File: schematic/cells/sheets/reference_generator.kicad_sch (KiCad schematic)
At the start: 10 parts, among them U1001 REF5050AIDR, U1004 OPA4197IPWR, U1007 OPA4197IPWR, U1010 OPA4197IPWR

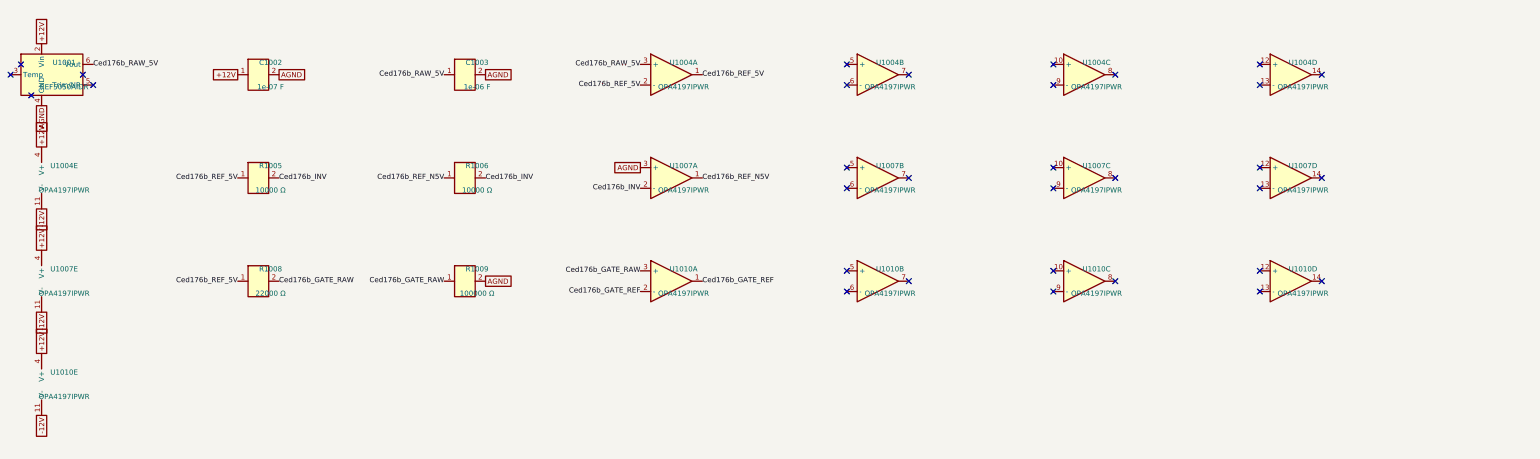
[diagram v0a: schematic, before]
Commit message: Close master schematic integration gates
Audit locked panel coverage, netlist parity, sensitive islands and all active units; terminate spare cells, refresh evidence, and record rail budget overshoot and draft exports.
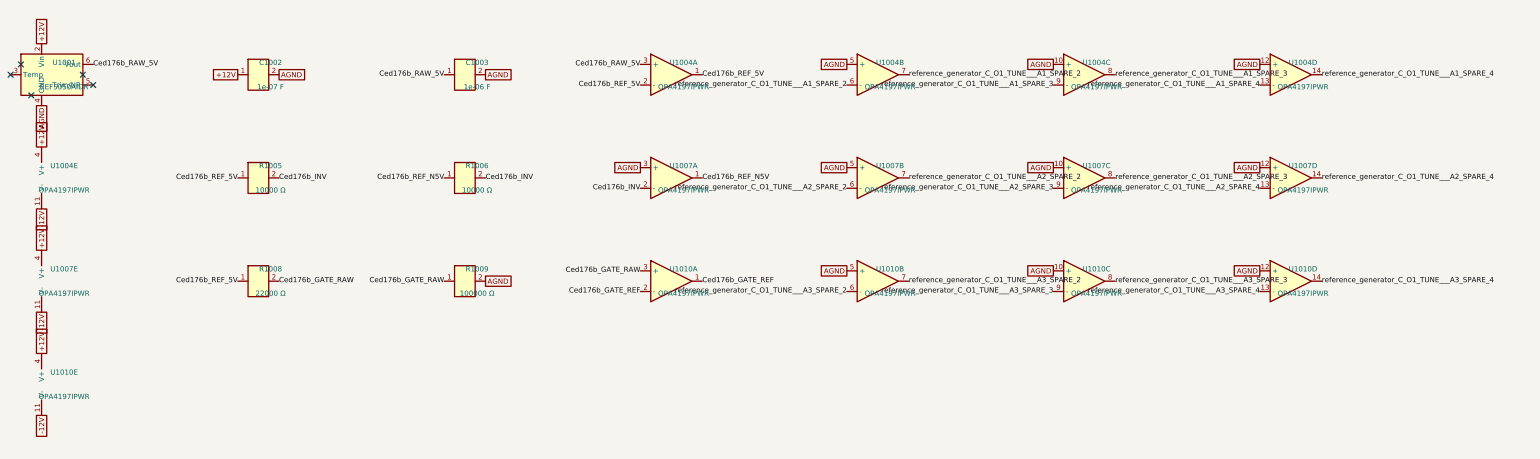
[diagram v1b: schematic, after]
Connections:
- net AGND: now also U1004.10 (+), U1004.12 (+), U1004.5 (+), U1007.10 (+), U1007.12 (+), U1007.5 (+), U1010.10 (+), U1010.12 (+), U1010.5 (+)
- net reference_generator_C_O1_TUNE___A1_SPARE_4: now reaches U1004.13 (-)
- net reference_generator_C_O1_TUNE___A1_SPARE_4: now also U1004.14
- net reference_generator_C_O1_TUNE___A2_SPARE_3: now reaches U1007.8
- net reference_generator_C_O1_TUNE___A2_SPARE_3: now also U1007.9 (-)
- net reference_generator_C_O1_TUNE___A3_SPARE_3: now reaches U1010.8
- net reference_generator_C_O1_TUNE___A3_SPARE_3: now also U1010.9 (-)
- net reference_generator_C_O1_TUNE___A2_SPARE_2: now reaches U1007.6 (-)
- net reference_generator_C_O1_TUNE___A2_SPARE_2: now also U1007.7
- net reference_generator_C_O1_TUNE___A1_SPARE_2: now reaches U1004.6 (-)
- net reference_generator_C_O1_TUNE___A1_SPARE_2: now also U1004.7
- net reference_generator_C_O1_TUNE___A1_SPARE_3: now reaches U1004.8
- net reference_generator_C_O1_TUNE___A1_SPARE_3: now also U1004.9 (-)
- net reference_generator_C_O1_TUNE___A3_SPARE_2: now reaches U1010.6 (-)
- net reference_generator_C_O1_TUNE___A3_SPARE_2: now also U1010.7
- net reference_generator_C_O1_TUNE___A2_SPARE_4: now reaches U1007.13 (-)
- net reference_generator_C_O1_TUNE___A2_SPARE_4: now also U1007.14
- net reference_generator_C_O1_TUNE___A3_SPARE_4: now reaches U1010.13 (-)
- net reference_generator_C_O1_TUNE___A3_SPARE_4: now also U1010.14
- no-connect marks 32 -> 5
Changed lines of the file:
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@@
     ))
   )
-  (no_connect (at 246.38 48.26))
-  (no_connect (at 246.38 53.34))
-  (no_connect (at 261.62 50.8))
+  (global_label "AGND" (shape passive) (at 246.38 48.26 0) (effects (font (size 1.27 1.27)) (justify right)))
+  (label "reference_generator_C_O1_TUNE___A1_SPARE_2" (at 246.38 53.34 0) (effects (font (size 1.27 1.27)) (justify right)))
+  (label "reference_generator_C_O1_TUNE___A1_SPARE_2" (at 261.62 50.8 180) (effects (font (size 1.27 1.27)) (justify left)))
   (symbol (lib_id "zudo-osc-hole-field:OPA4197IPWR") (at 304.8 50.8 0) (unit 3)
     (exclude_from_sim no) (in_bom yes) (on_board yes) (dnp no)
@@
     ))
   )
-  (no_connect (at 312.42 50.8))
-  (no_connect (at 297.18 53.34))
-  (no_connect (at 297.18 48.26))
+  (label "reference_generator_C_O1_TUNE___A1_SPARE_3" (at 312.42 50.8 180) (effects (font (size 1.27 1.27)) (justify left)))
+  (label "reference_generator_C_O1_TUNE___A1_SPARE_3" (at 297.18 53.34 0) (effects (font (size 1.27 1.27)) (justify right)))
+  (global_label "AGND" (shape passive) (at 297.18 48.26 0) (effects (font (size 1.27 1.27)) (justify right)))
   (symbol (lib_id "zudo-osc-hole-field:OPA4197IPWR") (at 355.6 50.8 0) (unit 4)
     (exclude_from_sim no) (in_bom yes) (on_board yes) (dnp no)
@@
     ))
   )
-  (no_connect (at 347.98 48.26))
-  (no_connect (at 347.98 53.34))
-  (no_connect (at 363.22 50.8))
+  (global_label "AGND" (shape passive) (at 347.98 48.26 0) (effects (font (size 1.27 1.27)) (justify right)))
+  (label "reference_generator_C_O1_TUNE___A1_SPARE_4" (at 347.98 53.34 0) (effects (font (size 1.27 1.27)) (justify right)))
+  (label "reference_generator_C_O1_TUNE___A1_SPARE_4" (at 363.22 50.8 180) (effects (font (size 1.27 1.27)) (justify left)))
   (symbol (lib_id "zudo-osc-hole-field:OPA4197IPWR") (at 50.8 76.2 0) (unit 5)
     (exclude_from_sim no) (in_bom yes) (on_board yes) (dnp no)
@@
     ))
   )
-  (no_connect (at 246.38 73.66))
-  (no_connect (at 246.38 78.74))
-  (no_connect (at 261.62 76.2))
+  (global_label "AGND" (shape passive) (at 246.38 73.66 0) (effects (font (size 1.27 1.27)) (justify right)))
+  (label "reference_generator_C_O1_TUNE___A2_SPARE_2" (at 246.38 78.74 0) (effects (font (size 1.27 1.27)) (justify right)))
+  (label "reference_generator_C_O1_TUNE___A2_SPARE_2" (at 261.62 76.2 180) (effects (font (size 1.27 1.27)) (justify left)))
   (symbol (lib_id "zudo-osc-hole-field:OPA4197IPWR") (at 304.8 76.2 0) (unit 3)
     (exclude_from_sim no) (in_bom yes) (on_board yes) (dnp no)
@@
     ))
   )
-  (no_connect (at 312.42 76.2))
-  (no_connect (at 297.18 78.74))
-  (no_connect (at 297.18 73.66))
+  (label "reference_generator_C_O1_TUNE___A2_SPARE_3" (at 312.42 76.2 180) (effects (font (size 1.27 1.27)) (justify left)))
+  (label "reference_generator_C_O1_TUNE___A2_SPARE_3" (at 297.18 78.74 0) (effects (font (size 1.27 1.27)) (justify right)))
+  (global_label "AGND" (shape passive) (at 297.18 73.66 0) (effects (font (size 1.27 1.27)) (justify right)))
   (symbol (lib_id "zudo-osc-hole-field:OPA4197IPWR") (at 355.6 76.2 0) (unit 4)
     (exclude_from_sim no) (in_bom yes) (on_board yes) (dnp no)
@@
     ))
   )
-  (no_connect (at 347.98 73.66))
-  (no_connect (at 347.98 78.74))
-  (no_connect (at 363.22 76.2))
+  (global_label "AGND" (shape passive) (at 347.98 73.66 0) (effects (font (size 1.27 1.27)) (justify right)))
+  (label "reference_generator_C_O1_TUNE___A2_SPARE_4" (at 347.98 78.74 0) (effects (font (size 1.27 1.27)) (justify right)))
+  (label "reference_generator_C_O1_TUNE___A2_SPARE_4" (at 363.22 76.2 180) (effects (font (size 1.27 1.27)) (justify left)))
   (symbol (lib_id "zudo-osc-hole-field:OPA4197IPWR") (at 50.8 101.6 0) (unit 5)
     (exclude_from_sim no) (in_bom yes) (on_board yes) (dnp no)
@@
     ))
   )
-  (no_connect (at 246.38 99.06))
-  (no_connect (at 246.38 104.14))
-  (no_connect (at 261.62 101.6))
+  (global_label "AGND" (shape passive) (at 246.38 99.06 0) (effects (font (size 1.27 1.27)) (justify right)))
+  (label "reference_generator_C_O1_TUNE___A3_SPARE_2" (at 246.38 104.14 0) (effects (font (size 1.27 1.27)) (justify right)))
+  (label "reference_generator_C_O1_TUNE___A3_SPARE_2" (at 261.62 101.6 180) (effects (font (size 1.27 1.27)) (justify left)))
   (symbol (lib_id "zudo-osc-hole-field:OPA4197IPWR") (at 304.8 101.6 0) (unit 3)
     (exclude_from_sim no) (in_bom yes) (on_board yes) (dnp no)
@@
     ))
   )
-  (no_connect (at 312.42 101.6))
-  (no_connect (at 297.18 104.14))
-  (no_connect (at 297.18 99.06))
+  (label "reference_generator_C_O1_TUNE___A3_SPARE_3" (at 312.42 101.6 180) (effects (font (size 1.27 1.27)) (justify left)))
+  (label "reference_generator_C_O1_TUNE___A3_SPARE_3" (at 297.18 104.14 0) (effects (font (size 1.27 1.27)) (justify right)))
+  (global_label "AGND" (shape passive) (at 297.18 99.06 0) (effects (font (size 1.27 1.27)) (justify right)))
   (symbol (lib_id "zudo-osc-hole-field:OPA4197IPWR") (at 355.6 101.6 0) (unit 4)
     (exclude_from_sim no) (in_bom yes) (on_board yes) (dnp no)
@@
     ))
   )
-  (no_connect (at 347.98 99.06))
-  (no_connect (at 347.98 104.14))
-  (no_connect (at 363.22 101.6))
+  (global_label "AGND" (shape passive) (at 347.98 99.06 0) (effects (font (size 1.27 1.27)) (justify right)))
+  (label "reference_generator_C_O1_TUNE___A3_SPARE_4" (at 347.98 104.14 0) (effects (font (size 1.27 1.27)) (justify right)))
+  (label "reference_generator_C_O1_TUNE___A3_SPARE_4" (at 363.22 101.6 180) (effects (font (size 1.27 1.27)) (justify left)))
   (symbol (lib_id "zudo-osc-hole-field:OPA4197IPWR") (at 50.8 127 0) (unit 5)
     (exclude_from_sim no) (in_bom yes) (on_board yes) (dnp no)
